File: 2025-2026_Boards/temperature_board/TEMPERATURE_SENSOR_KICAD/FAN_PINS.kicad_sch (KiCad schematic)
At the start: 16 parts, among them J12 Conn_01x02_Pin, J13 Conn_01x02_Pin, J14 Conn_01x02_Pin, J15 Conn_01x02_Pin, J16 Conn_01x02_Pin, J17 Conn_01x02_Pin, J18 Conn_01x02_Pin, J19 Conn_01x02_Pin, J2 Conn_01x02_Pin, J20 Conn_01x02_Pin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

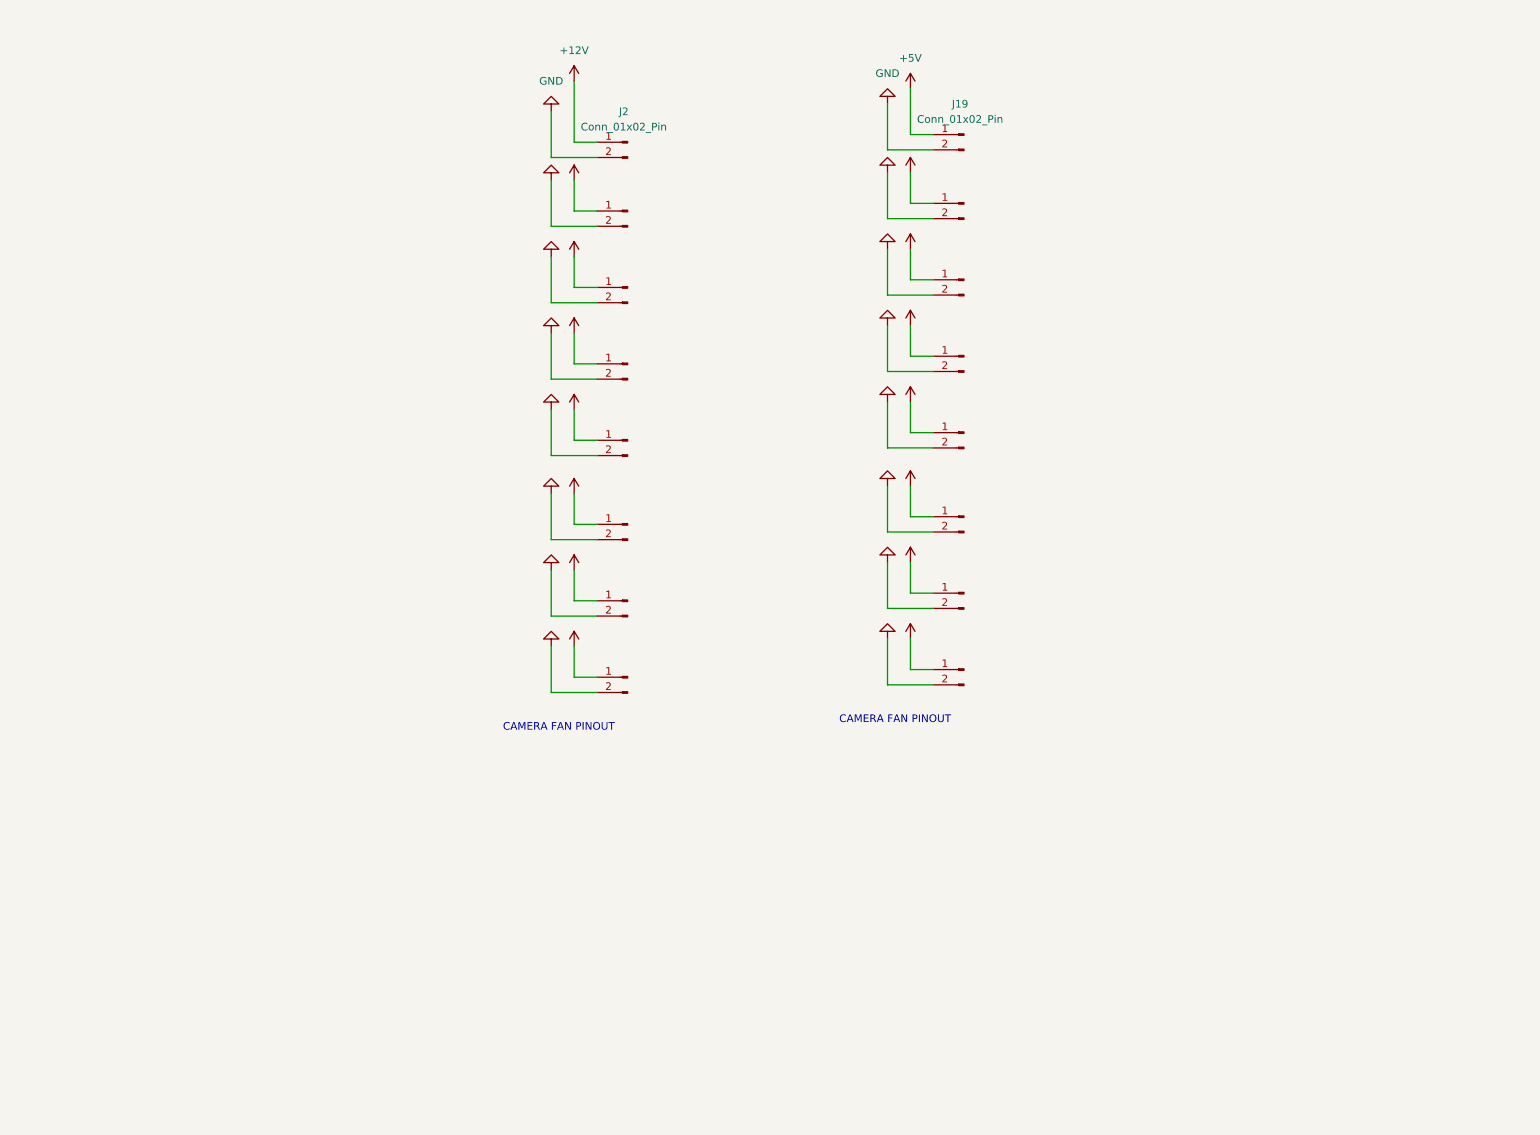
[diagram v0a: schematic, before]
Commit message: Worked on PCB. Have to change some track widths.
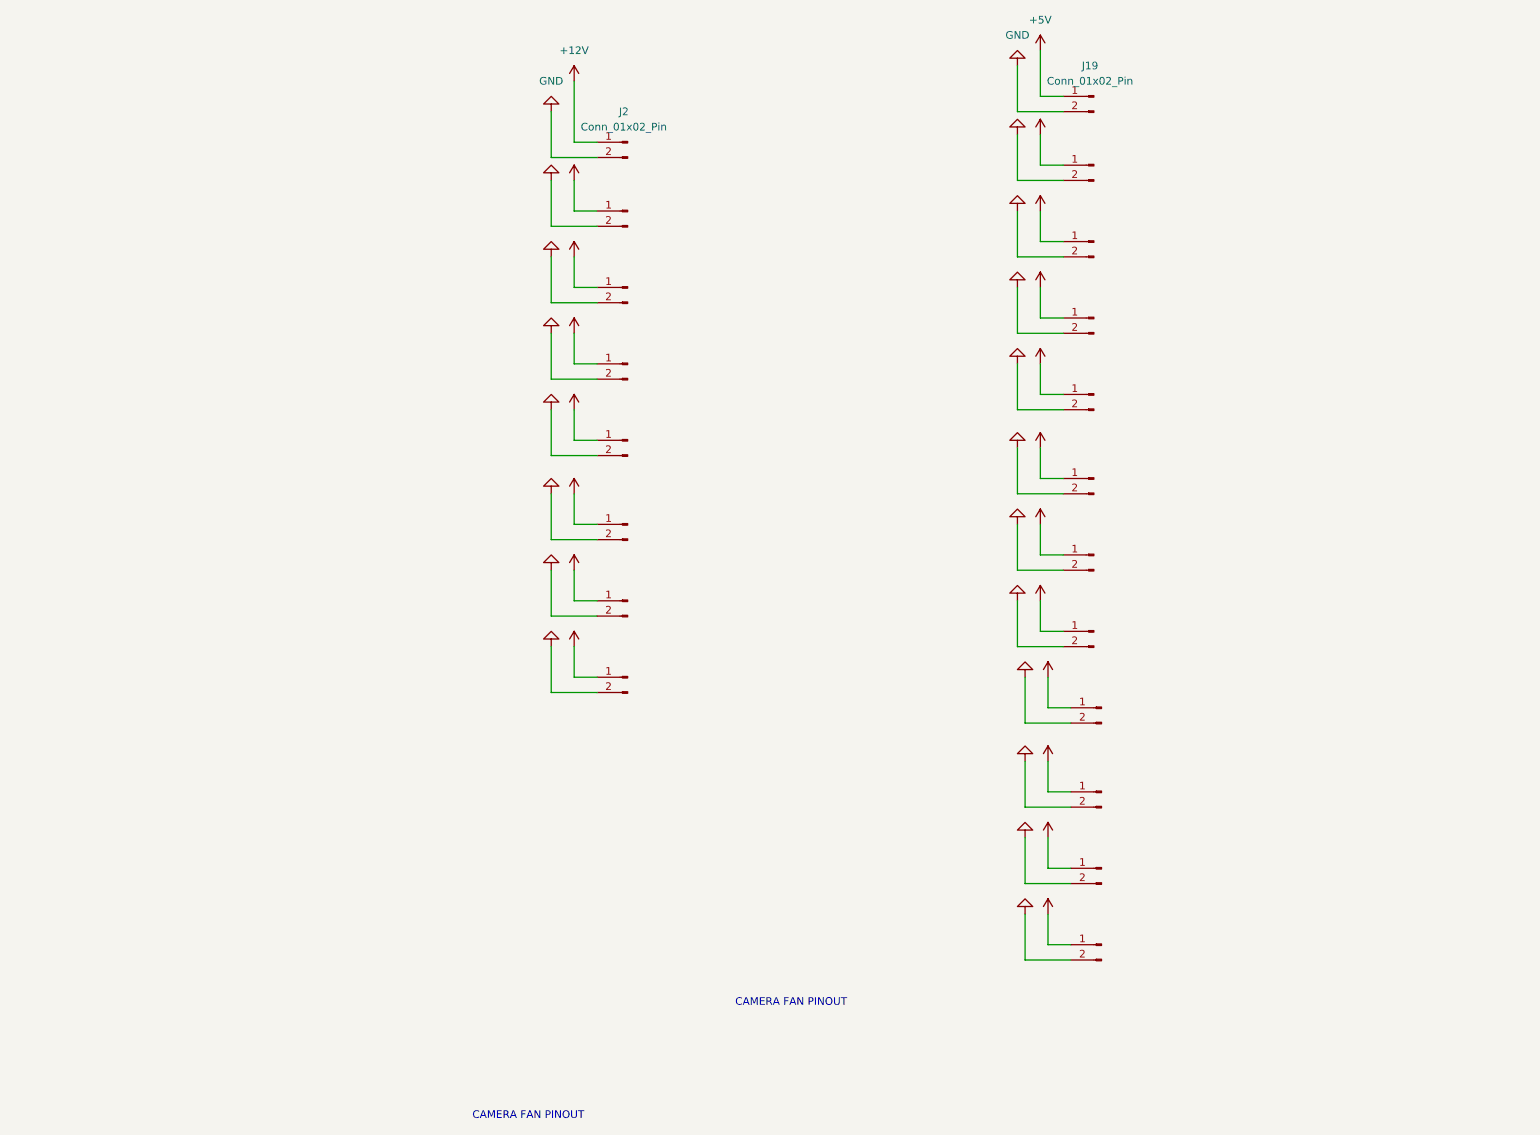
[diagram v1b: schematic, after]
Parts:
- added J4, J5, J6, J7: Conn_01x02_Pin, Connector_JST:JST_EH_B2B-EH-A_1x02_P2.50mm_Vertical, symbol Connector:Conn_01x02_Pin
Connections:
- net +5V: now also J4.1 (Pin_1), J5.1 (Pin_1), J6.1 (Pin_1), J7.1 (Pin_1)
- net GND: now also J4.2 (Pin_2), J5.2 (Pin_2), J6.2 (Pin_2), J7.2 (Pin_2)
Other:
- moved on the sheet: J19

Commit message: Fan connectors broken+buggy. Fixed it. Accidentally deleted ground plane. Will have to add back. To get done by start of work session on Sunday: Hook up all fan connectors. Hook up temperature sensor to microcontroller. Hook up power distributor to microcontroller. At work session: Figure out LCD-diode wiring
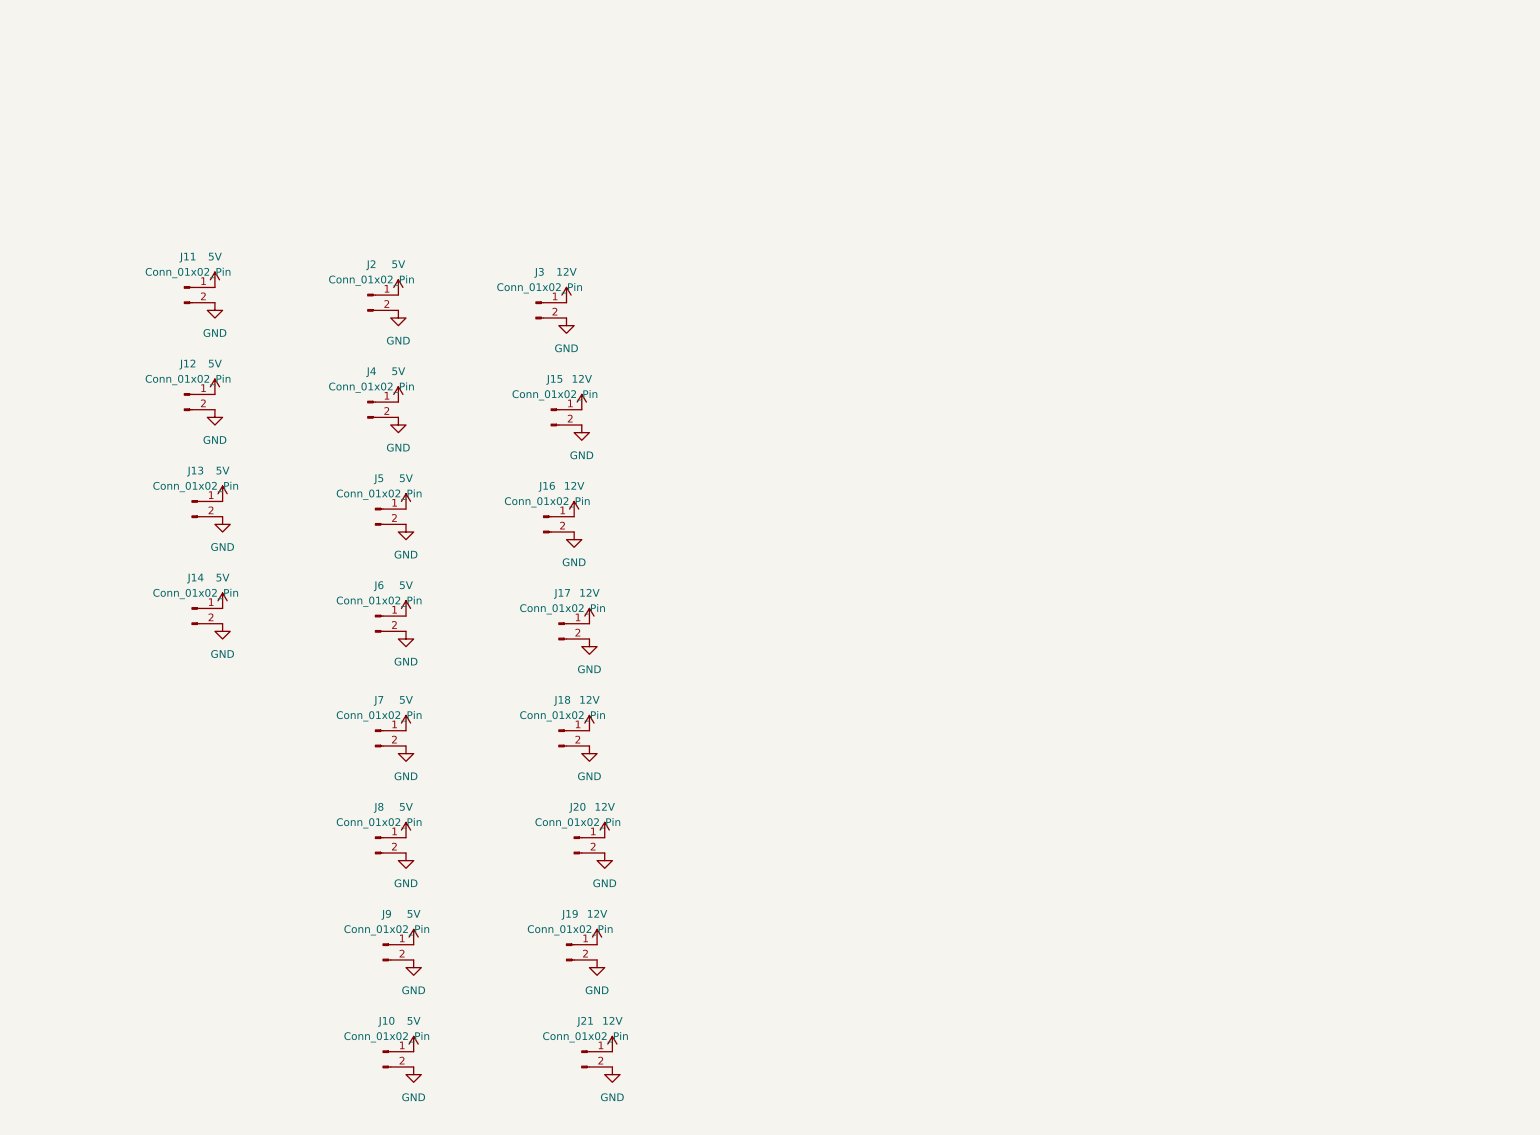
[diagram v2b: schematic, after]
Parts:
- removed J22, J23, J24, J25: Conn_01x02_Pin, Connector_JST:JST_EH_B2B-EH-A_1x02_P2.50mm_Vertical, symbol Connector:Conn_01x02_Pin
- added J10, J11, J8, J9: Conn_01x02_Pin, Connector:FanPinHeader_1x03_P2.54mm_Vertical, symbol Connector:Conn_01x02_Pin
- J12, J13, J14, J15, J16, J17, J18, J19, J2, J20, J21, J3, J4, J5, J6, J7: footprint Connector_JST:JST_EH_B2B-EH-A_1x02_P2.50mm_Vertical -> Connector:FanPinHeader_1x03_P2.54mm_Vertical
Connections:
- net GND: now also J10.2 (Pin_2), J11.2 (Pin_2), J8.2 (Pin_2), J9.2 (Pin_2)
- net +12V renamed 12V
- net 12V: now also J18.1 (Pin_1), J19.1 (Pin_1), J20.1 (Pin_1), J21.1 (Pin_1); no longer J12.1 (Pin_1), J13.1 (Pin_1), J14.1 (Pin_1), J2.1 (Pin_1)
- net +5V renamed 5V
- net 5V: now also J12.1 (Pin_1), J13.1 (Pin_1), J14.1 (Pin_1), J2.1 (Pin_1), J10.1 (Pin_1), J11.1 (Pin_1), J8.1 (Pin_1), J9.1 (Pin_1); no longer J18.1 (Pin_1), J19.1 (Pin_1), J20.1 (Pin_1), J21.1 (Pin_1)
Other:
- note removed: "CAMERA FAN PINOUT"

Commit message: Finishing up
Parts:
- J2: footprint Connector:FanPinHeader_1x03_P2.54mm_Vertical -> Connector_JST:JST_EH_S2B-EH_1x02_P2.50mm_Horizontal
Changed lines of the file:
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@@
 			)
 		)
-		(property "Footprint" "Connector:FanPinHeader_1x03_P2.54mm_Vertical"
+		(property "Footprint" "Connector_JST:JST_EH_S2B-EH_1x02_P2.50mm_Horizontal"
 			(at 88.9 58.42 0)
 			(effects

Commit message: minor updates
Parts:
- added C15, C16: 100n, Capacitor_SMD:C_0402_1005Metric, symbol Device:C
- added J24, J25: Conn_01x03_Socket, Connector_JST:JST_PH_S3B-PH-SM4-TB_1x03-1MP_P2.00mm_Horizontal, symbol Connector:Conn_01x03_Socket
- added U4: TCAN1057AEV-Q1, Package_SO:SOIC-8_3.9x4.9mm_P1.27mm, symbol moteus:TCAN1042HGVDRBRQ1
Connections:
- net 5V: now also C15.1, U4.3 (VCC)
- net GND: now also C15.2, C16.2, J24.3 (Pin_3), J25.3 (Pin_3), U4.2 (GND), U4.8 (STB), U4.9 (PAD)
- new net 3.3: C16.1, U4.5 (VIO)
- new net CAN+: J24.1 (Pin_1), J25.1 (Pin_1), U4.7 (CANH)
- new net CAN-: J24.2 (Pin_2), J25.2 (Pin_2), U4.6 (CANL)
- new net FDCAN_RX: U4.4 (RXD)
- new net FDCAN_TX: U4.1 (TXD)

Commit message: finishing the board. debuggign,ectc
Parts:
- added J22, J23: Conn_01x02_Pin, Connector_AMASS:AMASS_XT30PW-M_1x02_P2.50mm_Horizontal, symbol Connector:Conn_01x02_Pin
- J10, J11, J12, J13, J14, J15, J16, J17, J18, J19, J20, J21, J3, J4, J5, J6, J7, J8, J9: footprint Connector:FanPinHeader_1x03_P2.54mm_Vertical -> Connector_JST:JST_EH_S2B-EH_1x02_P2.50mm_Horizontal
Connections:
- net GND: now also J22.2 (Pin_2), J23.2 (Pin_2)
- net 3.3 renamed +3.3V
- new net 28V: J22.1 (Pin_1), J23.1 (Pin_1)

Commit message: finalizing board
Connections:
- net 12V is gone; now on net 5V: J15.1 (Pin_1), J16.1 (Pin_1), J17.1 (Pin_1), J18.1 (Pin_1), J19.1 (Pin_1), J20.1 (Pin_1), J21.1 (Pin_1), J3.1 (Pin_1)
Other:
- moved on the sheet: J15, J16, J17, J18, J19, J20, J21, J3

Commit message: updates
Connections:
- net FDCAN_RX renamed FDCAN_-
- net FDCAN_TX renamed FDCAN_+
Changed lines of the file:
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@@
 		)
 	)
-	(global_label "FDCAN_TX"
+	(global_label "FDCAN_+"
 		(shape input)
 		(at 167.64 81.28 180)
@@
 		)
 		(property "Intersheetrefs" "${INTERSHEET_REFS}"
-			(at 155.4624 81.28 0)
+			(at 156.0671 81.28 0)
 			(effects
 				(font
@@
 		)
 	)
-	(global_label "FDCAN_RX"
+	(global_label "FDCAN_-"
 		(shape input)
 		(at 167.64 91.44 180)
@@
 		)
 		(property "Intersheetrefs" "${INTERSHEET_REFS}"
-			(at 155.16 91.44 0)
+			(at 156.0671 91.44 0)
 			(effects
 				(font

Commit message: Finalized board
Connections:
- net CAN+: now also J25.2 (Pin_2); no longer J25.1 (Pin_1)
- net CAN-: now also J25.1 (Pin_1); no longer J25.2 (Pin_2)
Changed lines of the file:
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@@
 	(paper "A4")
 	(junction
-		(at 245.11 73.66)
-		(diameter 0)
-		(color 0 0 0 0)
-	)
-	(junction
-		(at 242.57 71.12)
+		(at 245.11 71.12)
 		(diameter 0)
 		(color 0 0 0 0)
@@
 		(color 0 0 0 0)
 	)
+	(junction
+		(at 242.57 73.66)
+		(diameter 0)
+		(color 0 0 0 0)
+	)
 	(wire
 		(pts
@@
 	(wire
 		(pts
-			(xy 234.95 73.66) (xy 245.11 73.66)
+			(xy 234.95 73.66) (xy 242.57 73.66)
 		)
 		(stroke
@@
 	(wire
 		(pts
-			(xy 245.11 83.82) (xy 245.11 73.66)
-		)
-		(stroke
-			(width 0)
-			(type default)
-		)
-	)
-	(wire
-		(pts
 			(xy 219.71 93.98) (xy 219.71 91.44)
 		)
@@
 	(wire
 		(pts
-			(xy 242.57 71.12) (xy 251.46 71.12)
+			(xy 232.41 71.12) (xy 245.11 71.12)
 		)
 		(stroke
@@
 	(wire
 		(pts
-			(xy 232.41 71.12) (xy 242.57 71.12)
-		)
-		(stroke
-			(width 0)
-			(type default)
-		)
-	)
-	(wire
-		(pts
-			(xy 242.57 81.28) (xy 242.57 71.12)
+			(xy 245.11 71.12) (xy 245.11 83.82)
 		)
 		(stroke
@@
 	(wire
 		(pts
-			(xy 245.11 73.66) (xy 251.46 73.66)
+			(xy 242.57 73.66) (xy 251.46 73.66)
 		)
 		(stroke
@@
 	(wire
 		(pts
+			(xy 242.57 73.66) (xy 242.57 81.28)
+		)
+		(stroke
+			(width 0)
+			(type default)
+		)
+	)
+	(wire
+		(pts
 			(xy 237.49 67.31) (xy 234.95 67.31)
 		)
@@
 	(wire
 		(pts
+			(xy 245.11 71.12) (xy 251.46 71.12)
+		)
+		(stroke
+			(width 0)
+			(type default)
+		)
+	)
+	(wire
+		(pts
 			(xy 219.71 91.44) (xy 231.14 91.44)
 		)
@@
 		(on_board yes)
 		(dnp no)
-		(fields_autoplaced yes)
 		(property "Reference" "J25"
-			(at 257.81 82.5499 0)
+			(at 258.826 88.392 0)
 			(effects
 				(font
@@
 		)
 		(property "Value" "Conn_01x03_Socket"
-			(at 257.81 85.0899 0)
+			(at 260.35 85.344 0)
 			(effects
 				(font
